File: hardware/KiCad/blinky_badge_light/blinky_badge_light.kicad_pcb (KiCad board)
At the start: 4 copper layers, 108.6 x 87.8 mm, 102 parts, among them Q2 Q_PMOS_GSD, SW1 TS-1187A-B-A-B, U1 ESP32-S3-WROOM-1 - no antenna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, U2 TP4056, U3 AP2112K-3.3, U4 MT3608, U5 CP2102N-Axx-xQFN24, U6 SN74LVC1T45DBV

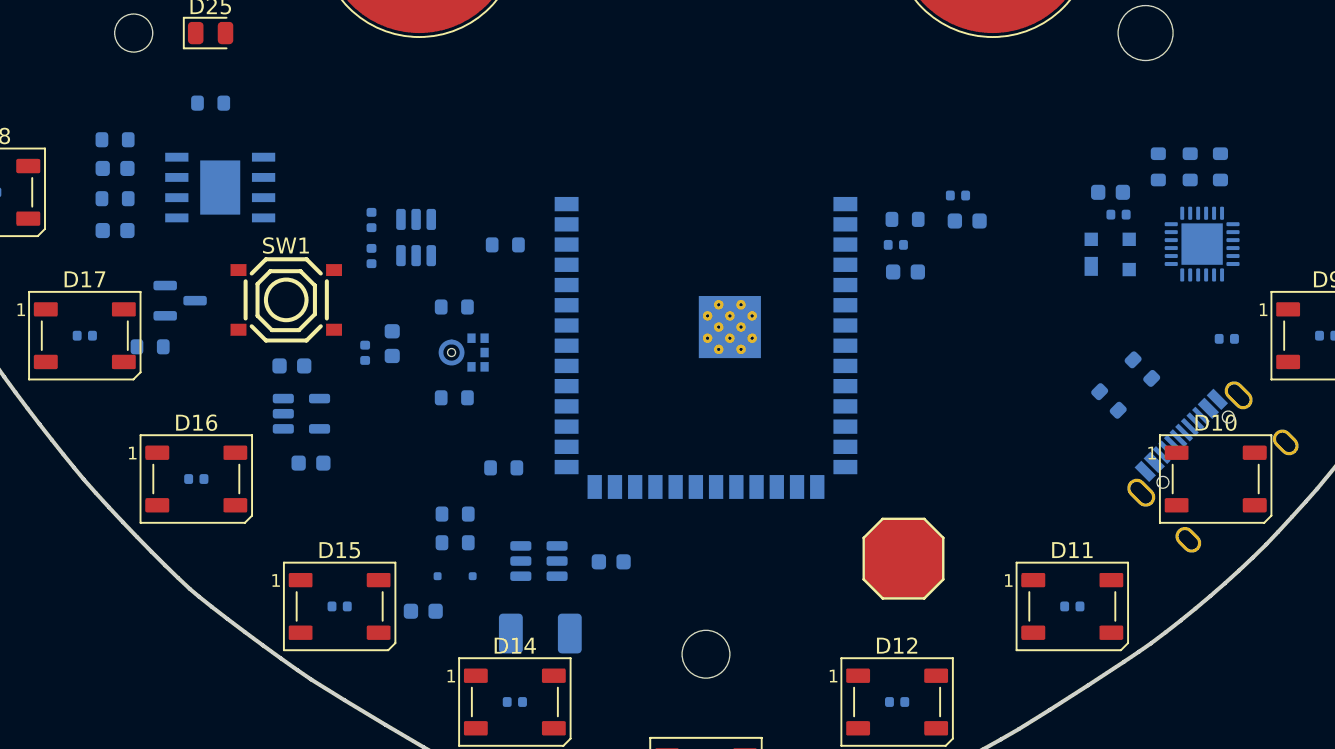
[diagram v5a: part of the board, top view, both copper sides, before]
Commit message: some initial slight mods
- improved USB signal layout
- reviewed boost regulator
- improved 3.3V power layout

still need to have a look at the overall USB power routing
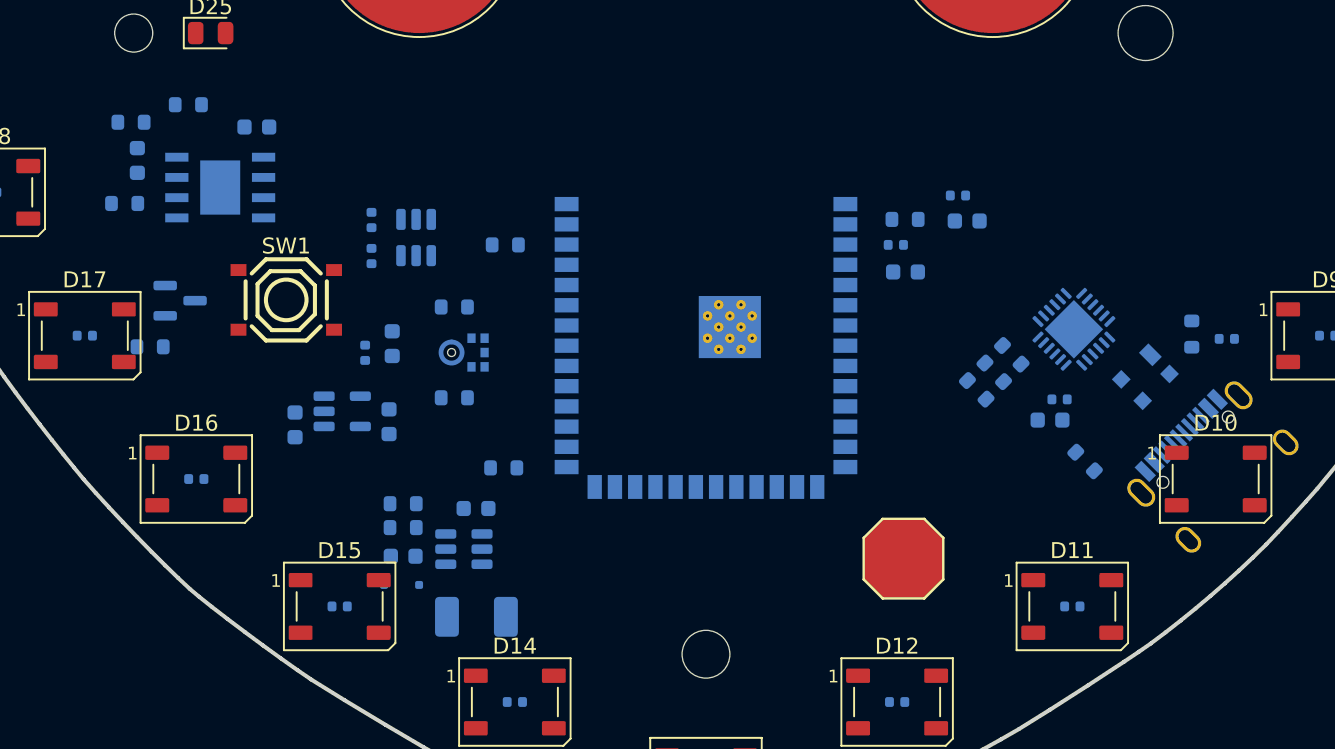
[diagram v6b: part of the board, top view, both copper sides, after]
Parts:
- moved R17 19.4 mm to (167.0, 111.4), turned to -45 degrees
- moved R10 17.6 mm to (169.2, 109.2), turned to -45 degrees
- moved R16 16.5 mm to (168.1, 110.3), turned to -45 degrees
- moved C30 14.8 mm to (171.6, 113.3)
- moved C29 12.2 mm to (172.2, 112.0)
- moved C33 11.0 mm to (121.8, 94.9)
- moved U5 9.67 mm to (173.1, 107.6), turned to 135 degrees
- moved C28 9.12 mm to (135.6, 118.8), turned to 180 degrees
- moved D27 7.98 mm to (177.6, 110.6), turned to -45 degrees
- moved C35 5.55 mm to (130.1, 113.4), turned to 90 degrees
- moved U4 4.77 mm to (134.8, 121.4)
- moved L1 4.15 mm to (135.6, 125.7)
- moved R6 4.09 mm to (173.8, 115.9)
- moved R5 3.80 mm to (180.5, 107.9), turned to -90 degrees
- moved C34 3.71 mm to (124.2, 113.6), turned to 90 degrees
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
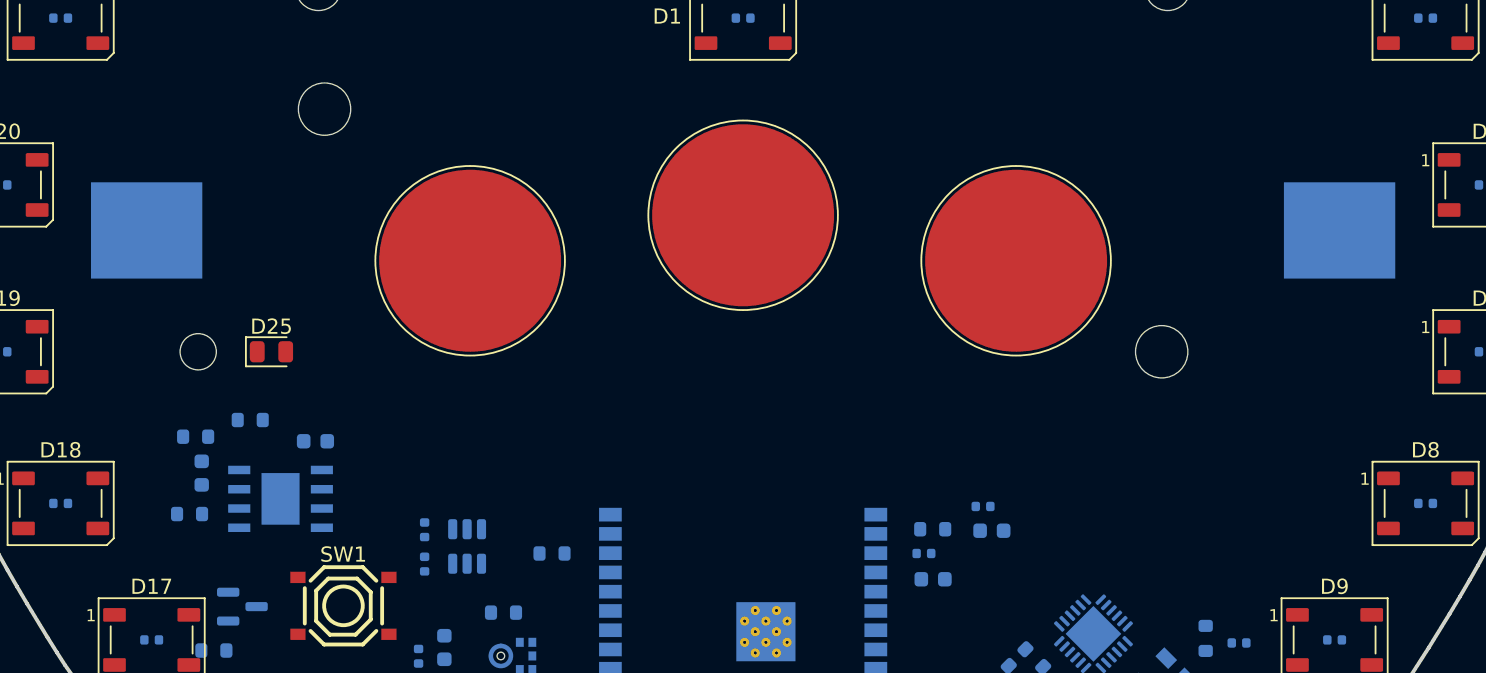
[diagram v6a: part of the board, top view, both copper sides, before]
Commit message: rotate battery, charger IC
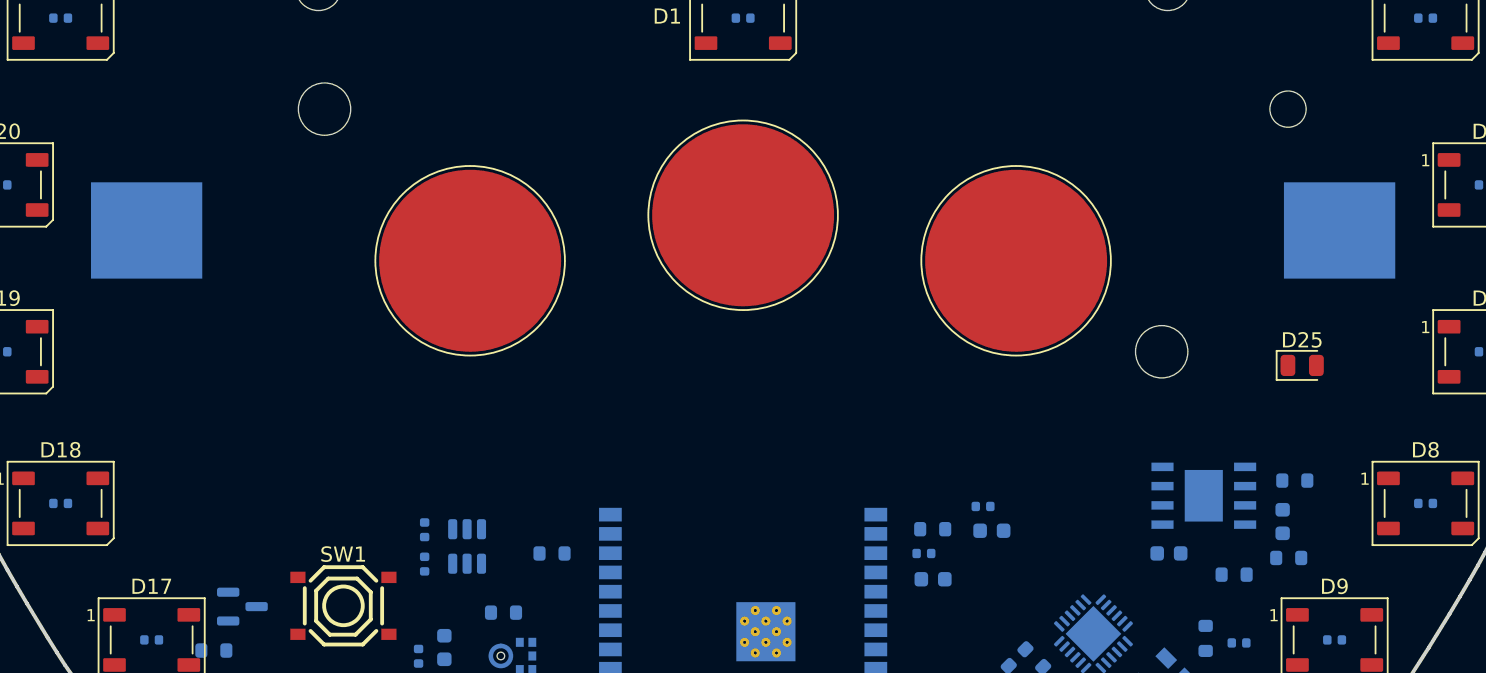
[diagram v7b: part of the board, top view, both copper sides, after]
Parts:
- moved R4 72.9 mm to (186.4, 97.5), turned to 0 degrees
- moved R3 72.5 mm to (186.0, 102.6), turned to 180 degrees
- moved C32 71.3 mm to (185.6, 100.2), turned to 90 degrees
- moved D25 68.0 mm to (186.9, 89.9)
- moved R14 65.7 mm to (182.4, 103.7), turned to 180 degrees
- moved U2 60.9 mm to (180.4, 98.5), turned to 180 degrees
- moved C33 56.8 mm to (178.1, 102.3), turned to 180 degrees
- turned BT1 to 180 degrees

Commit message: update with routing
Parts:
- U1: value ESP32-S3-WROOM-1 - no antenna keep out -> ESP32-S3-WROOM-1
- moved R9 81.5 mm to (194.0, 88.2), turned to 180 degrees
- moved Q2 78.3 mm to (193.9, 91.3), turned to -90 degrees
- moved SW1 66.5 mm to (188.4, 90.5), turned to -90 degrees
- moved L1 61.6 mm to (190.7, 98.2), turned to -90 degrees
- moved D26 61.5 mm to (188.7, 102.9), turned to 90 degrees
- moved C27 59.1 mm to (186.9, 102.8), turned to 90 degrees
- moved C34 57.4 mm to (180.4, 102.0), turned to -90 degrees
- moved U4 56.3 mm to (186.5, 99.0), turned to 90 degrees
- moved R7 56.2 mm to (184.5, 102.9), turned to 90 degrees
- moved R8 54.3 mm to (183.0, 102.9), turned to -90 degrees
- moved C28 52.6 mm to (183.9, 98.2), turned to -90 degrees
- moved U3 51.2 mm to (177.4, 102.8), turned to 180 degrees
- moved C35 45.8 mm to (174.5, 102.0), turned to -90 degrees
- moved TOUCH_4 41.7 mm to (123.9, 106.1)
- moved U6 37.0 mm to (143.3, 66.7)
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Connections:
- TOUCH_1 pad 1: Net-(U1-GPIO3/TOUCH3/ADC1_CH2) -> Net-(U1-GPIO5/TOUCH5/ADC1_CH4)
- TOUCH_2 pad 1: Net-(U1-GPIO4/TOUCH4/ADC1_CH3) -> Net-(U1-GPIO6/TOUCH6/ADC1_CH5)
- TOUCH_3 pad 1: Net-(U1-GPIO5/TOUCH5/ADC1_CH4) -> Net-(U1-GPIO3/TOUCH3/ADC1_CH2)
- TOUCH_4 pad 1: Net-(U1-GPIO6/TOUCH6/ADC1_CH5) -> Net-(U1-GPIO4/TOUCH4/ADC1_CH3)
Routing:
- net GND: track 0.00 -> 173.7 mm, vias 0 -> 66
- net 5V Power: track 0.00 -> 91.9 mm, vias 0 -> 29
- net LED DATA: track 0.00 -> 62.7 mm, vias 0 -> 2
- net ESP32 Reset: track 0.00 -> 50.7 mm, vias 0 -> 2
- net ESP32 Power Control: track 0.00 -> 47.4 mm, vias 0 -> 2
- net BAT+: track 0.00 -> 35.8 mm
- net Net-(U1-GPIO6/TOUCH6/ADC1_CH5): track 0.00 -> 34.6 mm, vias 0 -> 1
- net 3.3V Power: track 0.00 -> 31.2 mm, vias 0 -> 12
- net SYSTEM POWER: track 0.00 -> 31.1 mm
- net Net-(U1-GPIO3/TOUCH3/ADC1_CH2): track 0.00 -> 30.7 mm, vias 0 -> 1
- net Net-(U1-GPIO5/TOUCH5/ADC1_CH4): track 0.00 -> 29.2 mm, vias 0 -> 1
- net Net-(D25-K): track 0.00 -> 23.5 mm, vias 0 -> 1
- net ESP32 Boot: track 0.00 -> 21.2 mm, vias 0 -> 2
- net CP2102N TX → ESP32 RX: track 0.00 -> 20.7 mm
- net Net-(D1-DOUT): track 0.00 -> 20.3 mm
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- added copper zone on In1.Cu, net GND
- added copper zone on B.Cu, net Net-(D26-A)
- added copper zone on F.Cu, net USB Power
